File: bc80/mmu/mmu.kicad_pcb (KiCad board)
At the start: 2 copper layers, 62.2 x 55.9 mm, 9 parts, among them J1 Conn_01x06_Male, J2 Conn_01x03_Male, J3 Conn_01x03_Male, U1 74LS04, U2 74LS08, U3 74LS08, U4 74LS32, U5 74LS32, U6 74LS08

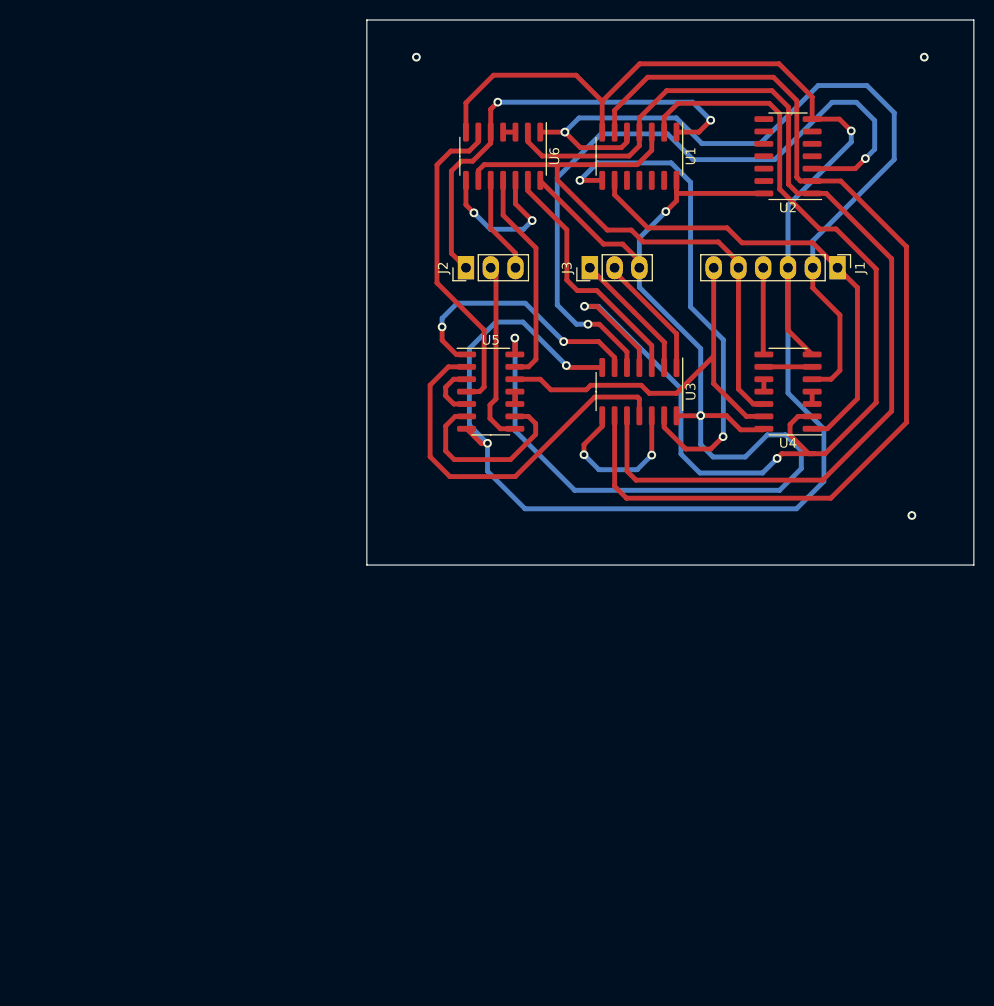
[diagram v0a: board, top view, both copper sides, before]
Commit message: a few fixes in MMU schematics and layout
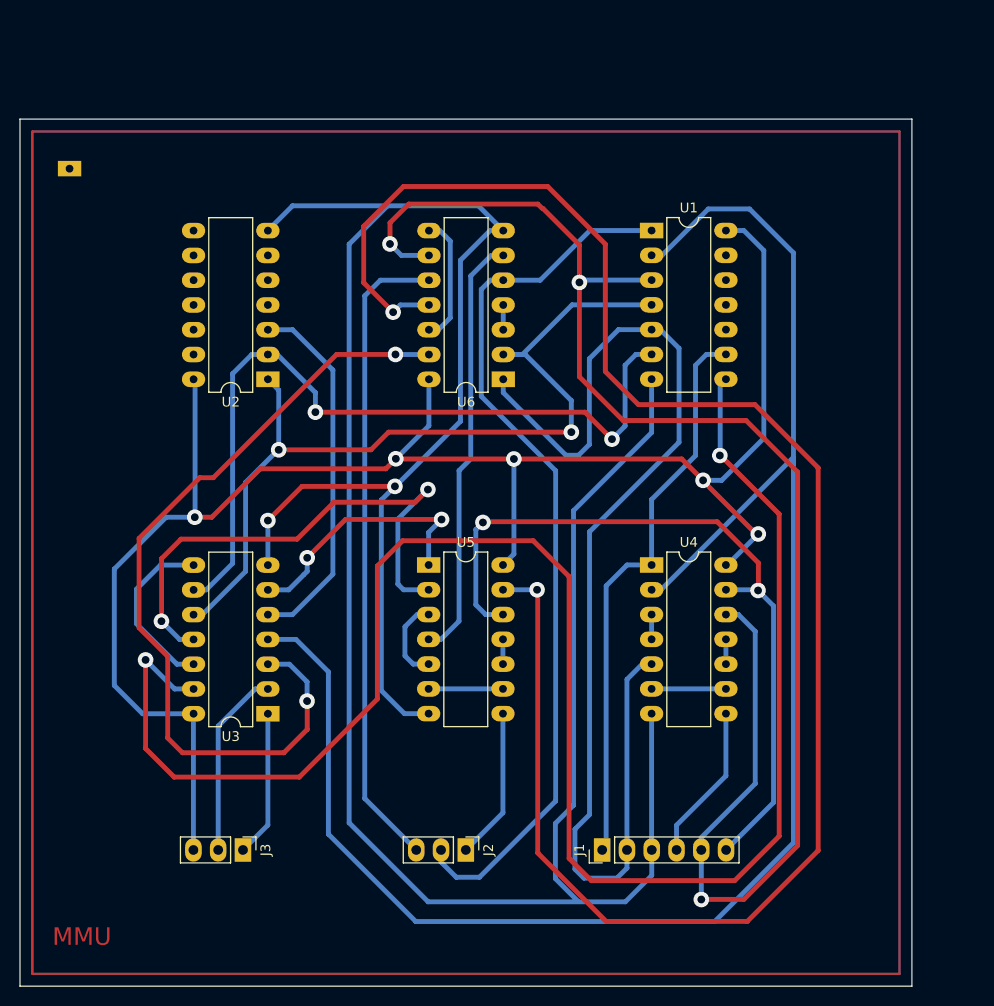
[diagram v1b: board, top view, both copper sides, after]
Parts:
- added ?: , , F.Cu at (91.4, 57.1)
- U1, U2, U3, U4, U5, U6: footprint Package_SO:SO-14_3.9x8.65mm_P1.27mm -> Package_DIP:DIP-14_W7.62mm_LongPads
- moved J3 69.5 mm to (109.2, 127.0), turned to -90 degrees
- moved J1 64.4 mm to (146.1, 127.0), turned to 90 degrees
- moved J2 59.7 mm to (132.1, 127.0), turned to -90 degrees
- moved U2 58.0 mm to (111.8, 78.7)
- moved U3 50.4 mm to (111.8, 113.0), turned to 180 degrees
- moved U6 22.9 mm to (135.9, 78.7), turned to 180 degrees
- moved U4 22.6 mm to (151.1, 97.8), turned to 0 degrees
- moved U5 18.9 mm to (128.3, 97.8)
- moved U1 7.72 mm to (151.1, 63.5), turned to 0 degrees
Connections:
- J2 pad 1: WR -> RAM_CS
- J2 pad 2: RAM_CS -> WR
- J3 pad 1: HIMEM_ON -> A13
- J3 pad 2: A13 -> HIMEM_ON
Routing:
- net Net-(U5-Pad13): track 22.2 -> 186.8 mm, vias 0 -> 2
- net Net-(U1-Pad8): track 51.4 -> 182.4 mm
- net GND: track 173.8 -> 279.7 mm, vias 3 -> 2
- net A15: track 61.3 -> 160.3 mm, vias 0 -> 3
- net Net-(U1-Pad2): track 109.3 -> 178.3 mm, vias 2 -> 0
- net Net-(U3-Pad3): track 25.6 -> 84.8 mm, vias 0 -> 2
- net +5V: track 123.7 -> 181.6 mm, vias 3 -> 5
- net A14: track 10.0 -> 66.2 mm
- net WR: track 46.9 -> 92.4 mm, vias 2 -> 0
- net MREQ: track 41.4 -> 77.4 mm, vias 0 -> 2
- net RD: track 84.1 -> 119.8 mm, vias 1 -> 0
- net Net-(U2-Pad3): track 72.7 -> 37.7 mm, vias 2 -> 0
- net Net-(U1-Pad6): track 104.3 -> 80.4 mm, vias 0 -> 2
- net Net-(U1-Pad4): track 106.8 -> 89.0 mm, vias 0 -> 2
- net Net-(U3-Pad11): track 39.3 -> 55.1 mm, vias 0 -> 2
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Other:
- board size 62.2 x 55.9 mm -> 91.4 x 88.9 mm
- board text added: "MMU"
